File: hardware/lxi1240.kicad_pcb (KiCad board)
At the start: 2 copper layers, 105.4 x 62.2 mm, 6 parts, among them J1 1240COMM, J2 1240COMM_EXT

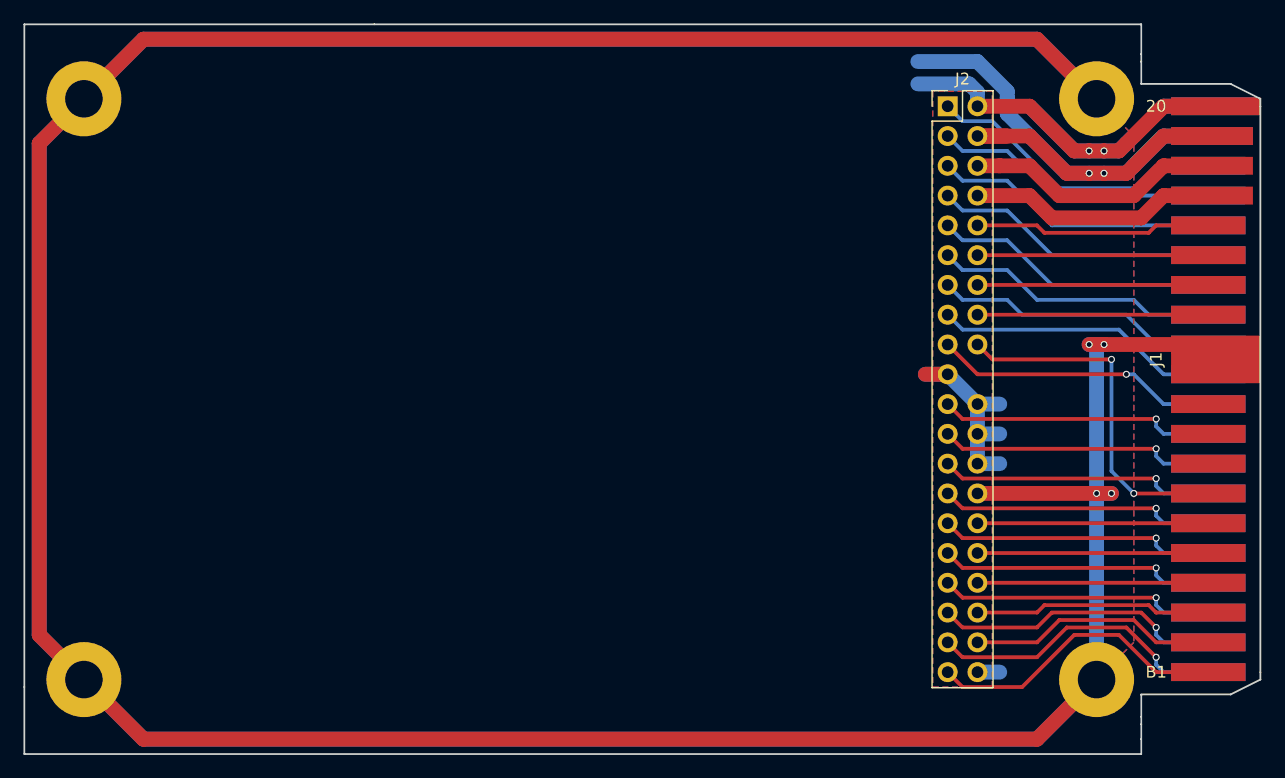
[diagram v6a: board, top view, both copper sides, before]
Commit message: Add fiducials and chamfer corners.
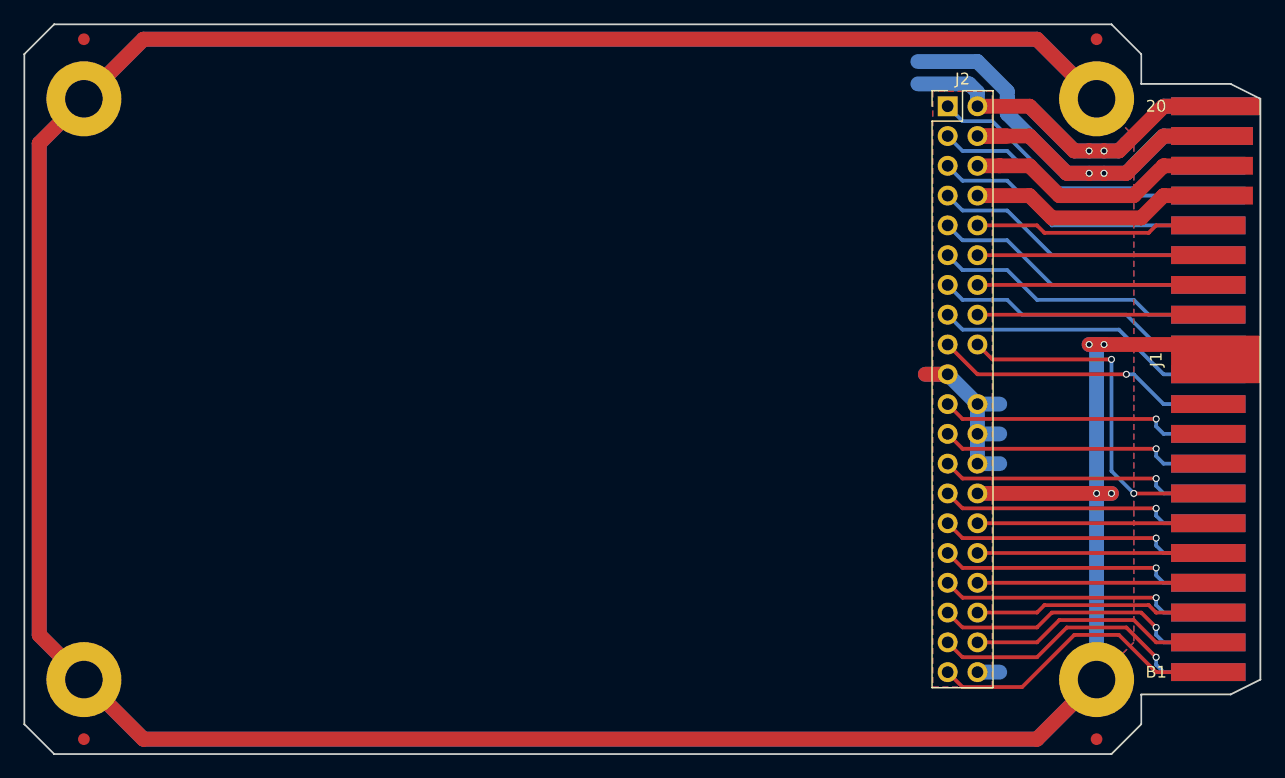
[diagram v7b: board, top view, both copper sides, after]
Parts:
- added FD1: Fiducial_1mm_Dia_2mm_Outer, Fiducials:Fiducial_1mm_Dia_2mm_Outer, F.Cu at (210.8, 118.7)
- added FD2: Fiducial_1mm_Dia_2mm_Outer, Fiducials:Fiducial_1mm_Dia_2mm_Outer, F.Cu at (124.5, 118.7)
- added FD3: Fiducial_1mm_Dia_2mm_Outer, Fiducials:Fiducial_1mm_Dia_2mm_Outer, F.Cu at (124.5, 59.1)
- added FD4: Fiducial_1mm_Dia_2mm_Outer, Fiducials:Fiducial_1mm_Dia_2mm_Outer, F.Cu at (210.8, 59.1)
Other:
- outline, holes or cut-outs redrawn
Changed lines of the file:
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@@
     (area 119.304999 57.709999 224.865001 120.090001)
     (thickness 1.6)
-    (drawings 63)
+    (drawings 59)
     (tracks 228)
     (zones 0)
-    (modules 6)
+    (modules 10)
     (nets 38)
   )
@@
     (pad_drill 1)
     (pad_to_mask_clearance 0.2)
-    (aux_axis_origin 0 0)
-    (visible_elements FFFEEB7F)
+    (aux_axis_origin 124.46 118.745)
+    (visible_elements FFFEFBFF)
     (pcbplotparams
-      (layerselection 0x00030_80000001)
+      (layerselection 0x010f0_80000001)
       (usegerberextensions false)
       (excludeedgelayer true)
@@
       (outputformat 1)
       (mirror false)
-      (drillshape 1)
+      (drillshape 0)
       (scaleselection 1)
       (outputdirectory ""))
@@
     (add_net Earth_Protective)
     (add_net GND)
+  )
+  (module Fiducials:Fiducial_1mm_Dia_2mm_Outer locked (layer F.Cu)
+    (at 124.46 118.745)
+    (descr "Circular Fiducial, 1mm bare copper top; 2mm keepout (Level A)")
+    (tags marker)
+    (attr virtual)
+    (fp_text reference FD2 (at 0 -2) (layer F.SilkS) hide
+      (effects (font (size 1 1) (thickness 0.15)))
+    )
+    (fp_text value Fiducial_1mm_Dia_2mm_Outer (at 0 2) (layer F.Fab)
+      (effects (font (size 1 1) (thickness 0.15)))
+    )
+    (fp_circle (center 0 0) (end 1 0) (layer F.Fab) (width 0.1))
+    (fp_text user %R (at 0 0) (layer F.Fab)
+      (effects (font (size 0.4 0.4) (thickness 0.06)))
+    )
+    (fp_circle (center 0 0) (end 1.25 0) (layer F.CrtYd) (width 0.05))
+    (pad ~ smd circle (at 0 0) (size 1 1) (layers F.Cu F.Mask)
+      (solder_mask_margin 0.5) (clearance 0.5))
+  )
+  (module Fiducials:Fiducial_1mm_Dia_2mm_Outer locked (layer F.Cu)
+    (at 124.46 59.055)
+    (descr "Circular Fiducial, 1mm bare copper top; 2mm keepout (Level A)")
+    (tags marker)
+    (attr virtual)
+    (fp_text reference FD3 (at 0 -2) (layer F.SilkS) hide
+      (effects (font (size 1 1) (thickness 0.15)))
+    )
+    (fp_text value Fiducial_1mm_Dia_2mm_Outer (at 0 2) (layer F.Fab)
+      (effects (font (size 1 1) (thickness 0.15)))
+    )
+    (fp_circle (center 0 0) (end 1 0) (layer F.Fab) (width 0.1))
+    (fp_text user %R (at 0 0) (layer F.Fab)
+      (effects (font (size 0.4 0.4) (thickness 0.06)))
+    )
+    (fp_circle (center 0 0) (end 1.25 0) (layer F.CrtYd) (width 0.05))
+    (pad ~ smd circle (at 0 0) (size 1 1) (layers F.Cu F.Mask)
+      (solder_mask_margin 0.5) (clearance 0.5))
+  )
+  (module Fiducials:Fiducial_1mm_Dia_2mm_Outer locked (layer F.Cu)
+    (at 210.82 118.745)
+    (descr "Circular Fiducial, 1mm bare copper top; 2mm keepout (Level A)")
+    (tags marker)
+    (attr virtual)
+    (fp_text reference FD1 (at 0 -2) (layer F.SilkS) hide
+      (effects (font (size 1 1) (thickness 0.15)))
+    )
+    (fp_text value Fiducial_1mm_Dia_2mm_Outer (at 0 2) (layer F.Fab)
+      (effects (font (size 1 1) (thickness 0.15)))
+    )
+    (fp_circle (center 0 0) (end 1 0) (layer F.Fab) (width 0.1))
+    (fp_text user %R (at 0 0) (layer F.Fab)
+      (effects (font (size 0.4 0.4) (thickness 0.06)))
+    )
+    (fp_circle (center 0 0) (end 1.25 0) (layer F.CrtYd) (width 0.05))
+    (pad ~ smd circle (at 0 0) (size 1 1) (layers F.Cu F.Mask)
+      (solder_mask_margin 0.5) (clearance 0.5))
   )
   (module 1240comm:1240COMM locked (layer F.Cu)
@@
     )
   )
+  (module Fiducials:Fiducial_1mm_Dia_2mm_Outer locked (layer F.Cu)
+    (at 210.82 59.055)
+    (descr "Circular Fiducial, 1mm bare copper top; 2mm keepout (Level A)")
+    (tags marker)
+    (attr virtual)
+    (fp_text reference FD4 (at 0 -2) (layer F.SilkS) hide
+      (effects (font (size 1 1) (thickness 0.15)))
+    )
+    (fp_text value Fiducial_1mm_Dia_2mm_Outer (at 0 2) (layer F.Fab)
+      (effects (font (size 1 1) (thickness 0.15)))
+    )
+    (fp_circle (center 0 0) (end 1 0) (layer F.Fab) (width 0.1))
+    (fp_text user %R (at 0 0) (layer F.Fab)
+      (effects (font (size 0.4 0.4) (thickness 0.06)))
+    )
+    (fp_circle (center 0 0) (end 1.25 0) (layer F.CrtYd) (width 0.05))
+    (pad ~ smd circle (at 0 0) (size 1 1) (layers F.Cu F.Mask)
+      (solder_mask_margin 0.5) (clearance 0.5))
+  )
+  (gr_line (start 214.63 117.475) (end 212.09 120.015) (layer Edge.Cuts) (width 0.15))
+  (gr_line (start 212.09 57.785) (end 214.63 60.325) (layer Edge.Cuts) (width 0.15))
+  (gr_line (start 119.38 60.325) (end 121.92 57.785) (layer Edge.Cuts) (width 0.15))
+  (gr_line (start 121.92 120.015) (end 119.38 117.475) (layer Edge.Cuts) (width 0.15))
+  (target plus (at 124.46 118.745) (size 5) (width 0.15) (layer Edge.Cuts))
   (gr_text "SOCKET EXTENDER\nUSE 80-CONDUCTOR ATA RIBBON" (at 210.185 88.9 270) (layer B.SilkS)
     (effects (font (size 1.5 1.5) (thickness 0.3)) (justify mirror))
@@
     (effects (font (size 1.5 1.5) (thickness 0.3)) (justify right mirror))
   )
-  (gr_line (start 119.38 114.3) (end 119.38 120.015) (angle 90) (layer Edge.Cuts) (width 0.15))
-  (gr_line (start 214.63 120.015) (end 119.38 120.015) (angle 90) (layer Edge.Cuts) (width 0.15))
-  (gr_line (start 119.38 57.785) (end 119.38 114.3) (angle 90) (layer Edge.Cuts) (width 0.15))
-  (gr_line (start 149.225 57.785) (end 119.38 57.785) (angle 90) (layer Edge.Cuts) (width 0.15))
+  (gr_line (start 212.09 120.015) (end 121.92 120.015) (angle 90) (layer Edge.Cuts) (width 0.15))
+  (gr_line (start 119.38 60.325) (end 119.38 117.475) (angle 90) (layer Edge.Cuts) (width 0.15))
   (dimension 95.25 (width 0.3) (layer Cmts.User)
     (gr_text "3.7500 in" (at 167.005 53.895) (layer Cmts.User)
@@
     (arrow2b (pts (xy 214.63 55.245) (xy 213.503496 55.831421)))
   )
-  (gr_line (start 214.63 57.785) (end 149.225 57.785) (angle 90) (layer Edge.Cuts) (width 0.15))
+  (gr_line (start 212.09 57.785) (end 121.92 57.785) (angle 90) (layer Edge.Cuts) (width 0.15))
   (dimension 62.23 (width 0.3) (layer Cmts.User)
     (gr_text "2.4500 in" (at 237.57 88.9 270) (layer Cmts.User)
@@
     (arrow2b (pts (xy 236.22 57.785) (xy 236.806421 58.911504)))
   )
-  (gr_line (start 214.63 118.745) (end 214.63 120.015) (angle 90) (layer Edge.Cuts) (width 0.15))
-  (gr_line (start 214.63 117.475) (end 214.63 118.745) (angle 90) (layer Edge.Cuts) (width 0.15))
-  (gr_line (start 214.63 60.325) (end 214.63 57.785) (angle 90) (layer Edge.Cuts) (width 0.15))
-  (gr_line (start 214.63 117.475) (end 214.63 116.84) (angle 90) (layer Edge.Cuts) (width 0.15))
-  (gr_line (start 214.63 60.96) (end 214.63 60.325) (angle 90) (layer Edge.Cuts) (width 0.15))
   (dimension 52.07 (width 0.3) (layer Cmts.User)
     (gr_text "2.0500 in" (at 232.49 88.9 270) (layer Cmts.User)
@@
     (arrow2b (pts (xy 231.14 62.865) (xy 231.726421 63.991504)))
   )
-  (gr_line (start 214.63 114.935) (end 214.63 116.84) (angle 90) (layer Edge.Cuts) (width 0.15))
-  (gr_line (start 214.63 62.865) (end 214.63 60.96) (angle 90) (layer Edge.Cuts) (width 0.15))
+  (gr_line (start 214.63 114.935) (end 214.63 117.475) (angle 90) (layer Edge.Cuts) (width 0.15))
+  (gr_line (start 214.63 62.865) (end 214.63 60.325) (angle 90) (layer Edge.Cuts) (width 0.15))
   (gr_line (start 222.25 62.865) (end 224.79 64.135) (angle 90) (layer Edge.Cuts) (width 0.15))
   (gr_line (start 222.25 114.935) (end 224.79 113.665) (angle 90) (layer Edge.Cuts) (width 0.15))
   (gr_line (start 214.63 114.935) (end 222.25 114.935) (angle 90) (layer Edge.Cuts) (width 0.15))
-  (gr_line (start 224.79 113.03) (end 224.79 113.665) (angle 90) (layer Edge.Cuts) (width 0.15))
-  (gr_line (start 224.79 64.135) (end 224.79 64.77) (angle 90) (layer Edge.Cuts) (width 0.15))
-  (gr_line (start 224.79 113.03) (end 224.79 64.77) (angle 90) (layer Edge.Cuts) (width 0.15))
+  (gr_line (start 224.79 113.665) (end 224.79 64.135) (angle 90) (layer Edge.Cuts) (width 0.15))
   (gr_line (start 222.25 62.865) (end 214.63 62.865) (angle 90) (layer Edge.Cuts) (width 0.15))
   (dimension 48.26 (width 0.3) (layer Cmts.User)

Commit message: Add CERN OHL license notices.
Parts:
- added Bonsai: Bonsai, 1240comm:Bonsai, F.Cu at (184.2, 80.6)
- added G***: LOGO, 1240comm:OSHW, B.Cu at (171.4, 80.0)
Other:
- board text added: "LXI Comm Pack for Tektronix 1240 v0.1 © 2017 Sam Hanes <sam@maltera.com> Licensed under CERN OHL v1.2 or newer Software under GNU GPL v3 or newer https://github.com/Elemecca/lxi1240"
- board text added: "SPFMDBC"
